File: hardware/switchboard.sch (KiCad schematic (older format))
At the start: 0 parts

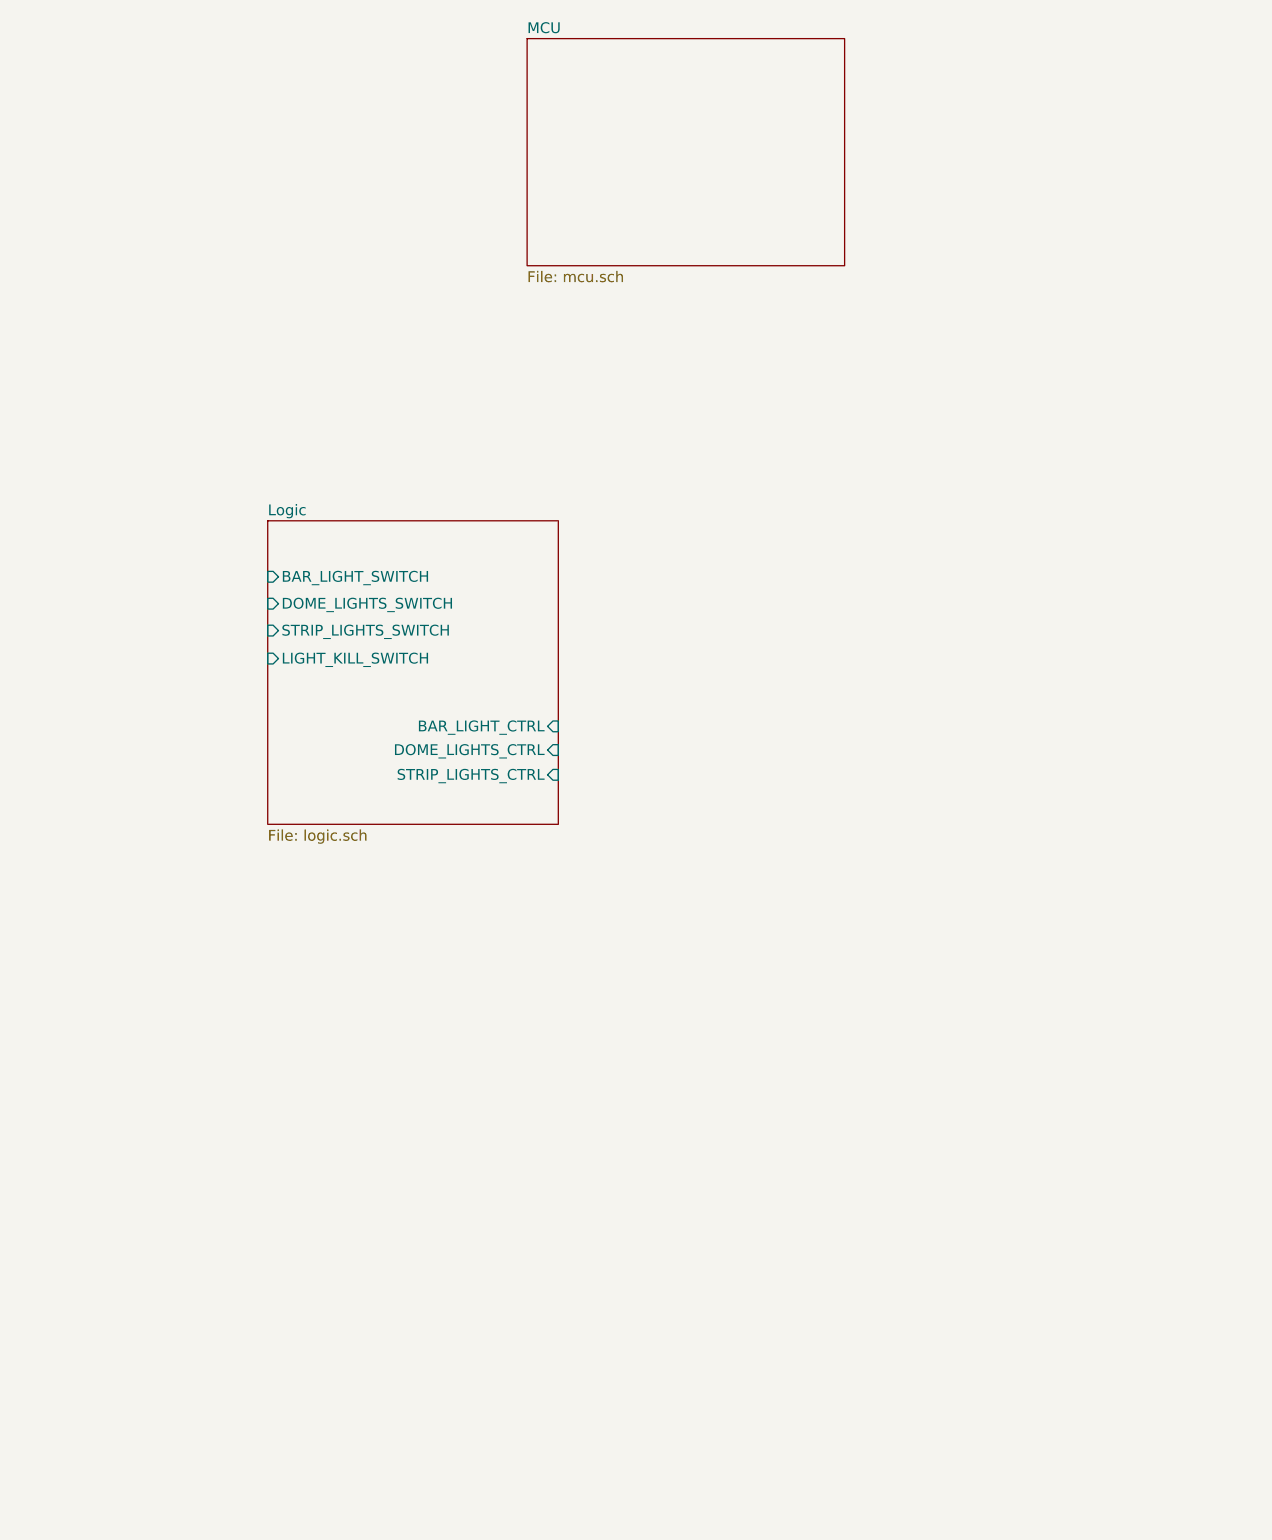
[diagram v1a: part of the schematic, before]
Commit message: hardware: add 5V domain for house and truck supplies
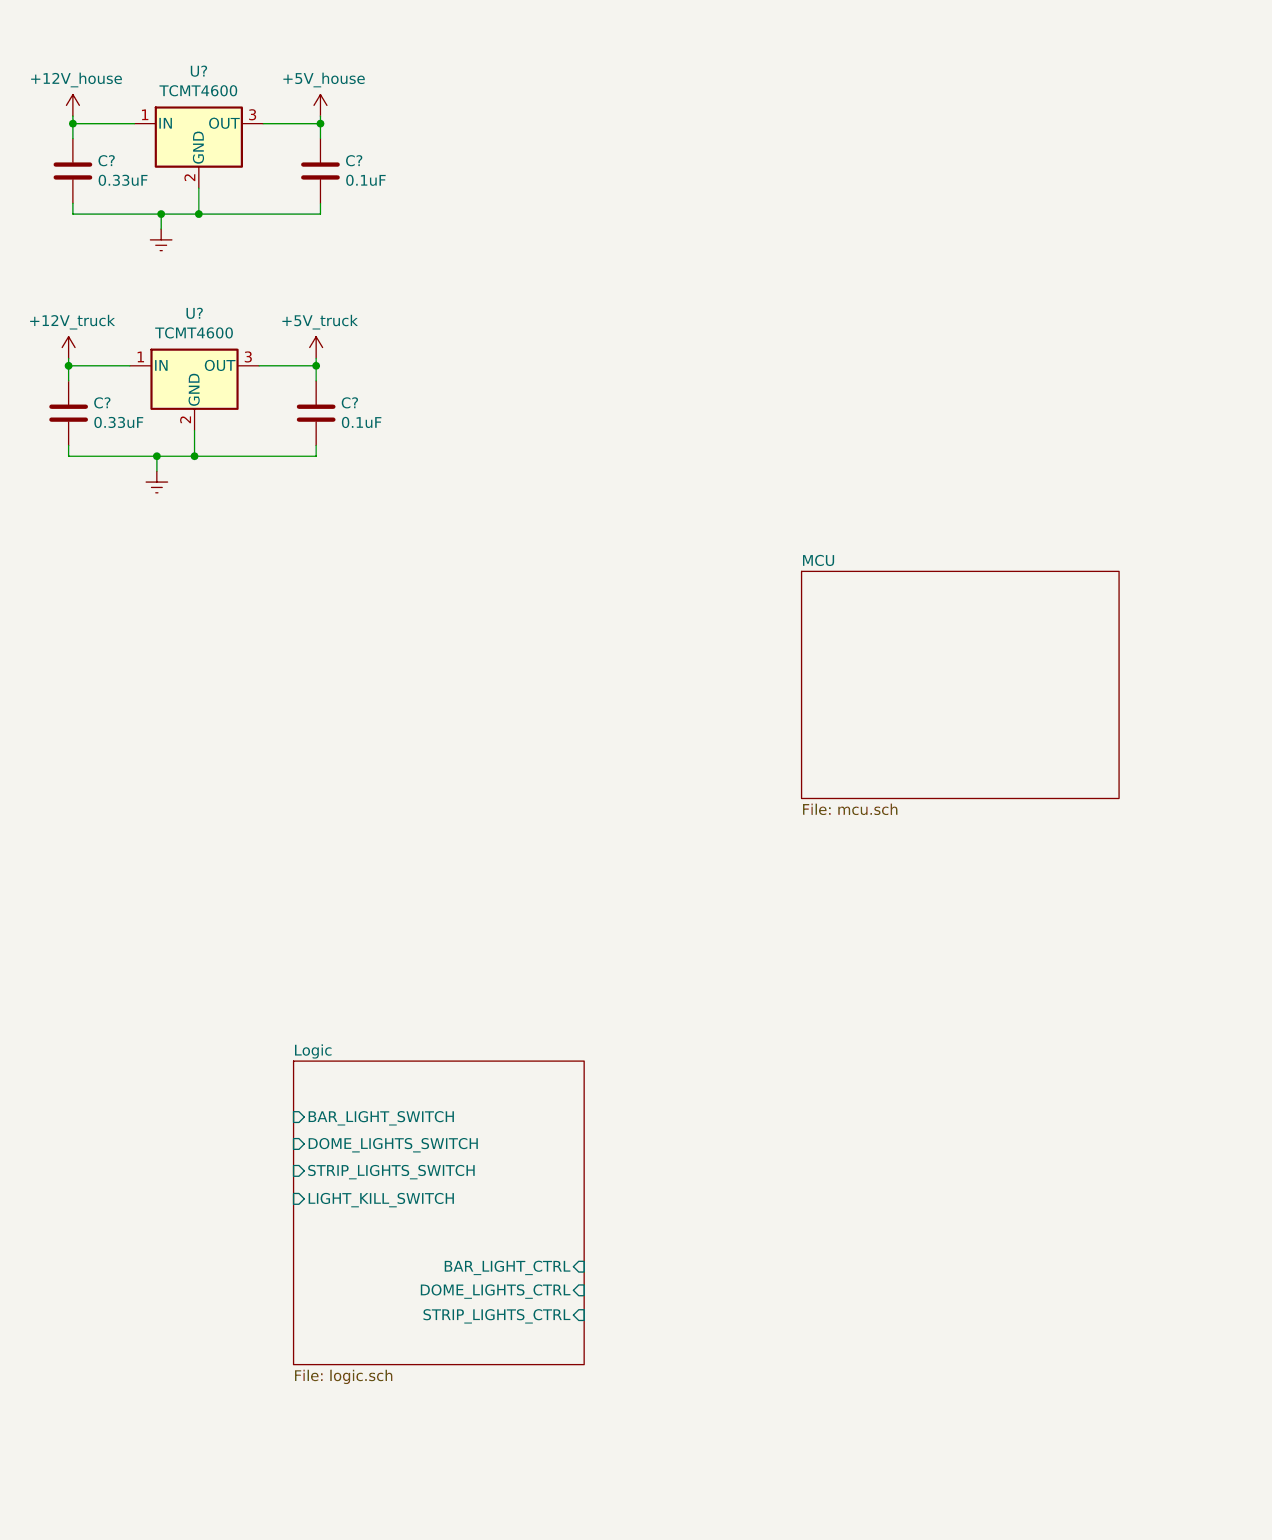
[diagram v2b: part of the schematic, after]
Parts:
- added C? (x2): 0.33uF, Capacitor_SMD:C_0805_2012Metric_Pad1.18x1.45mm_HandSolder, symbol Device:C
- added C? (x2): 0.1uF, Capacitor_SMD:C_0805_2012Metric_Pad1.18x1.45mm_HandSolder, symbol Device:C
- added U? (x2): TCMT4600, Package_SO:SOP-16_4.55x10.3mm_P1.27mm, symbol Regulator_Linear:L7805
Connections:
- new net +12V: C?.1, C?.1, U?.1 (IN), U?.1 (IN)
- new net +5V: C?.1, C?.1, U?.3 (OUT), U?.3 (OUT)
- new net GNDREF: C?.2, C?.2, C?.2, C?.2, U?.2 (GND), U?.2 (GND)
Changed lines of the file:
@@
 $EndDescr
 $Sheet
-S 2020 3100 1350 1410
+S 2140 5610 1350 1410
 U 606D525F
 F0 "Logic" 50
 F1 "logic.sch" 50
-F2 "BAR_LIGHT_CTRL" I R 3370 4055 50
-F3 "DOME_LIGHTS_CTRL" I R 3370 4165 50
-F4 "STRIP_LIGHTS_CTRL" I R 3370 4280 50
-F5 "BAR_LIGHT_SWITCH" I L 2020 3360 50
-F6 "DOME_LIGHTS_SWITCH" I L 2020 3485 50
-F7 "STRIP_LIGHTS_SWITCH" I L 2020 3610 50
-F8 "LIGHT_KILL_SWITCH" I L 2020 3740 50
+F2 "BAR_LIGHT_CTRL" I R 3490 6565 50
+F3 "DOME_LIGHTS_CTRL" I R 3490 6675 50
+F4 "STRIP_LIGHTS_CTRL" I R 3490 6790 50
+F5 "BAR_LIGHT_SWITCH" I L 2140 5870 50
+F6 "DOME_LIGHTS_SWITCH" I L 2140 5995 50
+F7 "STRIP_LIGHTS_SWITCH" I L 2140 6120 50
+F8 "LIGHT_KILL_SWITCH" I L 2140 6250 50
 $EndSheet
 $Sheet
-S 3225 860  1475 1055
+S 4500 3335 1475 1055
 U 60764D54
 F0 "MCU" 50
@@
 Wire Bus Line
 	12425 8055 11020 8055
+$Comp
+L Regulator_Linear:L7805 U?
+U 1 1 60B4A4D5
+P 1700 1255
+F 0 "U?" H 1700 1497 50  0000 C CNN
+F 1 "TCMT4600" H 1700 1406 50  0000 C CNN
+F 2 "Package_SO:SOP-16_4.55x10.3mm_P1.27mm" H 1725 1105 50  0001 L CIN
+F 3 "http://www.vishay.com/docs/83512/tcmt1600.pdf" H 1700 1205 50  0001 C CNN
+	1    1700 1255
+	1    0    0    -1
+$EndComp
+$Comp
+L Device:C C?
+U 1 1 60B4A4DB
+P 1115 1475
+F 0 "C?" H 1230 1521 50  0000 L CNN
+F 1 "0.33uF" H 1230 1430 50  0000 L CNN
+F 2 "Capacitor_SMD:C_0805_2012Metric_Pad1.18x1.45mm_HandSolder" H 1153 1325 50  0001 C CNN
+F 3 "~" H 1115 1475 50  0001 C CNN
+	1    1115 1475
+	1    0    0    -1
+$EndComp
+$Comp
+L Device:C C?
+U 1 1 60B4A4E1
+P 2265 1475
+F 0 "C?" H 2380 1521 50  0000 L CNN
+F 1 "0.1uF" H 2380 1430 50  0000 L CNN
+F 2 "Capacitor_SMD:C_0805_2012Metric_Pad1.18x1.45mm_HandSolder" H 2303 1325 50  0001 C CNN
+F 3 "~" H 2265 1475 50  0001 C CNN
+	1    2265 1475
+	1    0    0    -1
+$EndComp
+Wire Wire Line
+	2000 1255 2265 1255
+Wire Wire Line
+	1115 1255 1400 1255
+Wire Wire Line
+	1115 1625 1115 1675
+Wire Wire Line
+	1115 1675 1525 1675
+Wire Wire Line
+	2265 1675 2265 1625
+Connection ~ 1700 1675
+Wire Wire Line
+	1700 1675 2265 1675
+$Comp
+L power:GNDREF #PWR?
+U 1 1 60B4A4EE
+P 1525 1745
+AR Path="/605C1303/60B4A4EE" Ref="#PWR?"  Part="1"
+AR Path="/60B4A4EE" Ref="#PWR?"  Part="1"
+F 0 "#PWR?" H 1525 1495 50  0001 C CNN
+F 1 "GNDREF" H 1530 1572 50  0001 C CNN
+F 2 "" H 1525 1745 50  0001 C CNN
+F 3 "" H 1525 1745 50  0001 C CNN
+	1    1525 1745
+	1    0    0    -1
+$EndComp
+Wire Wire Line
+	1525 1745 1525 1675
+Connection ~ 1525 1675
+Wire Wire Line
+	1525 1675 1700 1675
+Wire Wire Line
+	1700 1555 1700 1675
+Wire Wire Line
+	1115 1255 1115 1325
+Wire Wire Line
+	2265 1255 2265 1325
+Wire Wire Line
+	2265 1255 2265 1220
+Connection ~ 2265 1255
+Wire Wire Line
+	1115 1255 1115 1220
+Connection ~ 1115 1255
+$Comp
+L switchboard:+12V_house #PWR?
+U 1 1 60B4A4FE
+P 1115 1220
+F 0 "#PWR?" H 1115 1070 50  0001 C CNN
+F 1 "+12V_house" H 1130 1393 50  0000 C CNN
+F 2 "" H 1115 1220 50  0001 C CNN
+F 3 "" H 1115 1220 50  0001 C CNN
+	1    1115 1220
+	1    0    0    -1
+$EndComp
+$Comp
+L Regulator_Linear:L7805 U?
+U 1 1 60B50BBB
+P 1680 2380
+F 0 "U?" H 1680 2622 50  0000 C CNN
+F 1 "TCMT4600" H 1680 2531 50  0000 C CNN
+F 2 "Package_SO:SOP-16_4.55x10.3mm_P1.27mm" H 1705 2230 50  0001 L CIN
+F 3 "http://www.vishay.com/docs/83512/tcmt1600.pdf" H 1680 2330 50  0001 C CNN
+	1    1680 2380
+	1    0    0    -1
+$EndComp
+$Comp
+L Device:C C?
+U 1 1 60B50BC1
+P 1095 2600
+F 0 "C?" H 1210 2646 50  0000 L CNN
+F 1 "0.33uF" H 1210 2555 50  0000 L CNN
+F 2 "Capacitor_SMD:C_0805_2012Metric_Pad1.18x1.45mm_HandSolder" H 1133 2450 50  0001 C CNN
+F 3 "~" H 1095 2600 50  0001 C CNN
+	1    1095 2600
+	1    0    0    -1
+$EndComp
+$Comp
+L Device:C C?
+U 1 1 60B50BC7
+P 2245 2600
+F 0 "C?" H 2360 2646 50  0000 L CNN
+F 1 "0.1uF" H 2360 2555 50  0000 L CNN
+F 2 "Capacitor_SMD:C_0805_2012Metric_Pad1.18x1.45mm_HandSolder" H 2283 2450 50  0001 C CNN
+F 3 "~" H 2245 2600 50  0001 C CNN
+	1    2245 2600
+	1    0    0    -1
+$EndComp
+Wire Wire Line
+	1980 2380 2245 2380
+Wire Wire Line
+	1095 2380 1380 2380
+Wire Wire Line
+	1095 2750 1095 2800
+Wire Wire Line
+	1095 2800 1505 2800
+Wire Wire Line
+	2245 2800 2245 2750
+Connection ~ 1680 2800
+Wire Wire Line
+	1680 2800 2245 2800
+$Comp
+L power:GNDREF #PWR?
+U 1 1 60B50BD4
+P 1505 2870
+AR Path="/605C1303/60B50BD4" Ref="#PWR?"  Part="1"
+AR Path="/60B50BD4" Ref="#PWR?"  Part="1"
+F 0 "#PWR?" H 1505 2620 50  0001 C CNN
+F 1 "GNDREF" H 1510 2697 50  0001 C CNN
+F 2 "" H 1505 2870 50  0001 C CNN
+F 3 "" H 1505 2870 50  0001 C CNN
+	1    1505 2870
+	1    0    0    -1
+$EndComp
+Wire Wire Line
+	1505 2870 1505 2800
+Connection ~ 1505 2800
+Wire Wire Line
+	1505 2800 1680 2800
+Wire Wire Line
+	1680 2680 1680 2800
+Wire Wire Line
+	1095 2380 1095 2450
+Wire Wire Line
+	2245 2380 2245 2450
+Wire Wire Line
+	2245 2380 2245 2345
+Connection ~ 2245 2380
+Wire Wire Line
+	1095 2380 1095 2345
+Connection ~ 1095 2380
+$Comp
+L switchboard:+5V_house #PWR?
+U 1 1 60B528AD
+P 2265 1220
+F 0 "#PWR?" H 2265 1070 50  0001 C CNN
+F 1 "+5V_house" H 2280 1393 50  0000 C CNN
+F 2 "" H 2265 1220 50  0001 C CNN
+F 3 "" H 2265 1220 50  0001 C CNN
+	1    2265 1220
+	1    0    0    -1
+$EndComp
+$Comp
+L switchboard:+5V_truck #PWR?
+U 1 1 60B53B6A
+P 2245 2345
+F 0 "#PWR?" H 2245 2195 50  0001 C CNN
+F 1 "+5V_truck" H 2260 2518 50  0000 C CNN
+F 2 "" H 2245 2345 50  0001 C CNN
+F 3 "" H 2245 2345 50  0001 C CNN
+	1    2245 2345
+	1    0    0    -1
+$EndComp
+$Comp
+L switchboard:+12V_truck #PWR?
+U 1 1 60B547E1
+P 1095 2345
+F 0 "#PWR?" H 1095 2195 50  0001 C CNN
+F 1 "+12V_truck" H 1110 2518 50  0000 C CNN
+F 2 "" H 1095 2345 50  0001 C CNN
+F 3 "" H 1095 2345 50  0001 C CNN
+	1    1095 2345
+	1    0    0    -1
+$EndComp
 $EndSCHEMATC

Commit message: hardware: use 5V_house/truck nets for load drivers
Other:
- note added: "TODO: use automotive safe regulator"
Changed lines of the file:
@@
 U 1 1 60B4A4D5
 P 1700 1255
+AR Path="/605C1303/60B4A4D5" Ref="U?"  Part="1"
+AR Path="/60B4A4D5" Ref="U?"  Part="1"
 F 0 "U?" H 1700 1497 50  0000 C CNN
 F 1 "TCMT4600" H 1700 1406 50  0000 C CNN
@@
 U 1 1 60B4A4DB
 P 1115 1475
+AR Path="/605C1303/60B4A4DB" Ref="C?"  Part="1"
+AR Path="/60B4A4DB" Ref="C?"  Part="1"
 F 0 "C?" H 1230 1521 50  0000 L CNN
 F 1 "0.33uF" H 1230 1430 50  0000 L CNN
@@
 U 1 1 60B4A4E1
 P 2265 1475
+AR Path="/605C1303/60B4A4E1" Ref="C?"  Part="1"
+AR Path="/60B4A4E1" Ref="C?"  Part="1"
 F 0 "C?" H 2380 1521 50  0000 L CNN
 F 1 "0.1uF" H 2380 1430 50  0000 L CNN
@@
 U 1 1 60B4A4FE
 P 1115 1220
+AR Path="/605C1303/60B4A4FE" Ref="#PWR?"  Part="1"
+AR Path="/60B4A4FE" Ref="#PWR?"  Part="1"
 F 0 "#PWR?" H 1115 1070 50  0001 C CNN
 F 1 "+12V_house" H 1130 1393 50  0000 C CNN
@@
 U 1 1 60B50BBB
 P 1680 2380
+AR Path="/605C1303/60B50BBB" Ref="U?"  Part="1"
+AR Path="/60B50BBB" Ref="U?"  Part="1"
 F 0 "U?" H 1680 2622 50  0000 C CNN
 F 1 "TCMT4600" H 1680 2531 50  0000 C CNN
@@
 U 1 1 60B50BC1
 P 1095 2600
+AR Path="/605C1303/60B50BC1" Ref="C?"  Part="1"
+AR Path="/60B50BC1" Ref="C?"  Part="1"
 F 0 "C?" H 1210 2646 50  0000 L CNN
 F 1 "0.33uF" H 1210 2555 50  0000 L CNN
@@
 U 1 1 60B50BC7
 P 2245 2600
+AR Path="/605C1303/60B50BC7" Ref="C?"  Part="1"
+AR Path="/60B50BC7" Ref="C?"  Part="1"
 F 0 "C?" H 2360 2646 50  0000 L CNN
 F 1 "0.1uF" H 2360 2555 50  0000 L CNN
@@
 	1    0    0    -1
 $EndComp
+Text Notes 2605 2445 0    50   ~ 0
+TODO: use automotive safe regulator
 $EndSCHEMATC

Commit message: hardware: use MIC2940A for 5V supplies
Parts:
- removed U? (x2): TCMT4600, Package_SO:SOP-16_4.55x10.3mm_P1.27mm, symbol Regulator_Linear:L7805
- added U? (x2): MIC2940A, Package_TO_SOT_SMD:TO-263-3_TabPin4, symbol switchboard:MIC2940A
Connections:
- net +12V: now also U?.1 (IN), U?.1 (IN)
- net +5V: now also U?.3 (OUT), U?.3 (OUT)
- net GNDREF: now also U?.2 (GND), U?.2 (GND)
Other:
- note removed: "TODO: use automotive safe regulator"
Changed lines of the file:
@@
 	12425 8055 11020 8055
-$Comp
-L Regulator_Linear:L7805 U?
-U 1 1 60B4A4D5
-P 1700 1255
-AR Path="/605C1303/60B4A4D5" Ref="U?"  Part="1"
-AR Path="/60B4A4D5" Ref="U?"  Part="1"
-F 0 "U?" H 1700 1497 50  0000 C CNN
-F 1 "TCMT4600" H 1700 1406 50  0000 C CNN
-F 2 "Package_SO:SOP-16_4.55x10.3mm_P1.27mm" H 1725 1105 50  0001 L CIN
-F 3 "http://www.vishay.com/docs/83512/tcmt1600.pdf" H 1700 1205 50  0001 C CNN
-	1    1700 1255
-	1    0    0    -1
-$EndComp
 $Comp
 L Device:C C?
@@
 $EndComp
 $Comp
-L Regulator_Linear:L7805 U?
-U 1 1 60B50BBB
-P 1680 2380
-AR Path="/605C1303/60B50BBB" Ref="U?"  Part="1"
-AR Path="/60B50BBB" Ref="U?"  Part="1"
-F 0 "U?" H 1680 2622 50  0000 C CNN
-F 1 "TCMT4600" H 1680 2531 50  0000 C CNN
-F 2 "Package_SO:SOP-16_4.55x10.3mm_P1.27mm" H 1705 2230 50  0001 L CIN
-F 3 "http://www.vishay.com/docs/83512/tcmt1600.pdf" H 1680 2330 50  0001 C CNN
-	1    1680 2380
-	1    0    0    -1
-$EndComp
-$Comp
 L Device:C C?
 U 1 1 60B50BC1
@@
 	1    0    0    -1
 $EndComp
-Text Notes 2605 2445 0    50   ~ 0
-TODO: use automotive safe regulator
+$Comp
+L switchboard:MIC2940A U?
+U 1 1 60A42020
+P 1700 1255
+F 0 "U?" H 1700 1497 50  0000 C CNN
+F 1 "MIC2940A" H 1700 1406 50  0000 C CNN
+F 2 "Package_TO_SOT_SMD:TO-263-3_TabPin4" H 1725 1105 50  0001 L CIN
+F 3 "http://www.st.com/content/ccc/resource/technical/document/datasheet/41/4f/b3/b0/12/d4/47/88/CD00000444.pdf/files/CD00000444.pdf/jcr:content/translations/en.CD00000444.pdf" H 1700 1205 50  0001 C CNN
+	1    1700 1255
+	1    0    0    -1
+$EndComp
+$Comp
+L switchboard:MIC2940A U?
+U 1 1 60A433DF
+P 1680 2380
+F 0 "U?" H 1680 2622 50  0000 C CNN
+F 1 "MIC2940A" H 1680 2531 50  0000 C CNN
+F 2 "Package_TO_SOT_SMD:TO-263-3_TabPin4" H 1705 2230 50  0001 L CIN
+F 3 "http://www.st.com/content/ccc/resource/technical/document/datasheet/41/4f/b3/b0/12/d4/47/88/CD00000444.pdf/files/CD00000444.pdf/jcr:content/translations/en.CD00000444.pdf" H 1680 2330 50  0001 C CNN
+	1    1680 2380
+	1    0    0    -1
+$EndComp
 $EndSCHEMATC
